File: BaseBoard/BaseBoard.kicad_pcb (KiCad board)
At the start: 2 copper layers, 100 x 86 mm, 48 parts, among them J1 Raspberry_Pi_2_3, J10 Conn_01x01, J11 Conn_01x01, J12 Conn_01x02_Female, J13 Conn_01x02_Female, J14 Conn_01x02_Female, J15 USB_C_Receptacle_USB2.0, J16 Conn_01x02_Female, J17 MOTOR, J18 MOTOR, J19 MOTOR, J2 Longan_A, J20 MOTOR, J21 Conn_01x01, J22 Conn_01x01, J23 IMU, J3 TB6612_A, J4 TB6612_A, J5 Longan_C, J6 Longan_B, J7 TB6612_B, J8 TB6612_B, J9 Conn_02x04, U1 SY6912, U2 CH224K

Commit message: v2板临时提交
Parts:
- removed J11: Conn_01x01, Connector_PinHeader_2.54mm:PinHeader_1x01_P2.54mm_Vertical
- removed J12, J13: Conn_01x02_Female, Connector_Molex:Molex_Mini-Fit_Jr_5566-02A_2x01_P4.20mm_Vertical
- removed J17, J18, J19, J20: MOTOR, Connector_JST:JST_PH_B6B-PH-K_1x06_P2.00mm_Vertical
- removed J6: Longan_B, Connector_PinSocket_2.54mm:PinSocket_1x18_P2.54mm_Vertical
- removed U1: SY6912, Package_SO:HSOP-8-1EP_3.9x4.9mm_P1.27mm_EP2.41x3.1mm_ThermalVias
- added C10: 100nF, Capacitor_SMD:C_0805_2012Metric, F.Cu at (169.7, 30.6)
- added C11: 10uF, Capacitor_SMD:CP_Elec_4x5.4, F.Cu at (139.5, 135.8)
- added C12: 100nF, Capacitor_SMD:C_0805_2012Metric, F.Cu at (134.5, 135.7)
- added C13: 10uF, Capacitor_SMD:CP_Elec_4x5.4, F.Cu at (139.5, 128.4)
- added C14: 100nF, Capacitor_SMD:C_0805_2012Metric, F.Cu at (134.5, 131.6)
- added C15: 10uF, Capacitor_SMD:CP_Elec_4x5.4, F.Cu at (139.5, 121.4)
- added C16: 100nF, Capacitor_SMD:C_0805_2012Metric, F.Cu at (134.5, 121.6)
- added C17: 10uF, Capacitor_SMD:CP_Elec_4x5.4, F.Cu at (139.5, 114.4)
- added C18: 100nF, Capacitor_SMD:C_0805_2012Metric, F.Cu at (134.5, 114.6)
- added C19: 6pF, Capacitor_SMD:C_0603_1608Metric, F.Cu at (131.6, 96.7)
- added C20: 6pF, Capacitor_SMD:C_0603_1608Metric, F.Cu at (178.0, 129.1)
- added C21: 6pF, Capacitor_SMD:C_0603_1608Metric, F.Cu at (129.3, 96.7)
- added C22: 6pF, Capacitor_SMD:C_0603_1608Metric, F.Cu at (185.2, 128.9)
- added C23: 100nF, Capacitor_SMD:C_0805_2012Metric, F.Cu at (173.4, 133.7)
- added C24: 100nF, Capacitor_SMD:C_0805_2012Metric, F.Cu at (180.3, 142.7)
- added C25: 100nF, Capacitor_SMD:C_0805_2012Metric, F.Cu at (173.4, 130.7)
- added C26: 100nF, Capacitor_SMD:C_0805_2012Metric, F.Cu at (158.7, 141.8)
- added C27: 100nF, Capacitor_SMD:C_0805_2012Metric, F.Cu at (175.9, 142.7)
- added C28: 100nF, Capacitor_SMD:C_0805_2012Metric, F.Cu at (158.7, 144.8)
- added C5: 105, Capacitor_SMD:C_0805_2012Metric, F.Cu at (141.1, 78.1)
- added C6: 220uF, Capacitor_SMD:CP_Elec_8x10, F.Cu at (147.2, 74.7)
- added C7: 33nF, Capacitor_SMD:C_0805_2012Metric, F.Cu at (160.9, 91.2)
- added C8: 220uF, Capacitor_SMD:CP_Elec_8x10, F.Cu at (139.3, 95.2)
- added C9: 105, Capacitor_SMD:C_0805_2012Metric, F.Cu at (145.8, 91.6)
- added D4: SS54, Diode_SMD:D_SMB, F.Cu at (156.3, 76.0)
- added D5: LED_Red, LED_SMD:LED_0805_2012Metric, F.Cu at (208.6, 100.6)
- added K1: G5LE-1, Relay_THT:Relay_SPDT_Omron-G5LE-1, F.Cu at (102.5, 79.7)
- added L2: 33uH, Inductor_SMD:L_10.4x10.4_H4.8, F.Cu at (157.5, 83.9)
- added R10: 100k, Resistor_SMD:R_0805_2012Metric, F.Cu at (127.0, 94.2)
- added R11: 360k, Resistor_SMD:R_0805_2012Metric, F.Cu at (122.5, 97.2)
- added R12: 5.1k, Resistor_SMD:R_0805_2012Metric, F.Cu at (177.5, 112.1)
- added R13: 22R, Resistor_SMD:R_0805_2012Metric, F.Cu at (177.5, 115.1)
- added R14: 22R, Resistor_SMD:R_0805_2012Metric, F.Cu at (170.6, 123.5)
- added R15: 10k, Resistor_SMD:R_0805_2012Metric, F.Cu at (181.9, 112.1)
- added R16: 10k, Resistor_SMD:R_0805_2012Metric, F.Cu at (177.5, 118.0)
- added R17: 0, Resistor_SMD:R_0805_2012Metric, F.Cu at (181.9, 115.1)
- added R18: 0, Resistor_SMD:R_0805_2012Metric, F.Cu at (175.0, 123.5)
- added R19: 10k, Resistor_SMD:R_0805_2012Metric, F.Cu at (186.3, 112.1)
- added R20: 10k, Resistor_SMD:R_0805_2012Metric, F.Cu at (181.9, 118.0)
- added R8: 28k, Resistor_SMD:R_0805_2012Metric, F.Cu at (157.1, 91.2)
- added R9: 2k, Resistor_SMD:R_0805_2012Metric, F.Cu at (153.8, 91.2)
- added SW1: SW_Push, Button_Switch_SMD:SW_SPST_TL3342, F.Cu at (156.4, 65.8)
- added SW2: SW_Push, Button_Switch_SMD:SW_SPST_TL3342, F.Cu at (147.2, 65.8)
- added U3: XL4005, Package_TO_SOT_SMD:TO-263-5_TabPin3, F.Cu at (143.3, 84.9)
- added U4: TB6612FNG, Package_SO:SSOP-24_5.3x8.2mm_P0.65mm, F.Cu at (126.5, 118.6)
- added U5: TB6612FNG, Package_SO:SSOP-24_5.3x8.2mm_P0.65mm, F.Cu at (126.5, 132.6)
- added U6: GD32VF103Cx, Package_QFP:LQFP-48_7x7mm_P0.5mm, F.Cu at (128.5, 103.6)
- added Y1: 32.768k, Crystal:Crystal_C38-LF_D3.0mm_L8.0mm_Horizontal, F.Cu at (131.5, 93.6)
- added Y2: 8Mhz, Crystal:Crystal_SMD_5032-2Pin_5.0x3.2mm, F.Cu at (182.6, 124.8)
- C2: value 470nF -> 1uF
- C3: value 10uF/X7R -> 470nF
- C4: value 1uF -> 10uF/X7R
- J10: value Conn_01x01 -> MOTOR; footprint Connector_PinHeader_2.54mm:PinHeader_1x01_P2.54mm_Vertical -> Connector_JST:JST_PH_B6B-PH-K_1x06_P2.00mm_Vertical
- J14: footprint Connector_AMASS:AMASS_XT60-M_1x02_P7.20mm_Vertical -> Connector_Molex:Molex_Mini-Fit_Jr_5566-02A_2x01_P4.20mm_Vertical
- J15: value USB_C_Receptacle_USB2.0 -> Conn_01x02_Female; footprint Connector_USB:USB_C_Receptacle_HRO_TYPE-C-31-M-12 -> Connector_Molex:Molex_Mini-Fit_Jr_5566-02A_2x01_P4.20mm_Vertical
- J16: footprint Connector_Molex:Molex_Mini-Fit_Jr_5566-02A_2x01_P4.20mm_Vertical -> Connector_AMASS:AMASS_XT60-M_1x02_P7.20mm_Vertical
- J2: value Longan_A -> USB_C_Receptacle_USB2.0; footprint Connector_PinSocket_2.54mm:PinSocket_1x18_P2.54mm_Vertical -> Connector_USB:USB_C_Receptacle_HRO_TYPE-C-31-M-12
- J21: value Conn_01x01 -> Conn_01x02_Female; footprint Connector_PinHeader_2.54mm:PinHeader_1x01_P2.54mm_Vertical -> Connector_Molex:Molex_Mini-Fit_Jr_5566-02A_2x01_P4.20mm_Vertical
- J22: value Conn_01x01 -> USB_C_Receptacle_USB2.0; footprint Connector_PinHeader_2.54mm:PinHeader_1x01_P2.54mm_Vertical -> Connector_USB:USB_C_Receptacle_HRO_TYPE-C-31-M-12
- J3: value TB6612_A -> Conn_01x04; footprint Connector_PinSocket_2.54mm:PinSocket_1x08_P2.54mm_Vertical -> Connector_JST:JST_PH_B4B-PH-K_1x04_P2.00mm_Vertical
- J4: value TB6612_A -> MOTOR; footprint Connector_PinSocket_2.54mm:PinSocket_1x08_P2.54mm_Vertical -> Connector_JST:JST_PH_B6B-PH-K_1x06_P2.00mm_Vertical
- J5: value Longan_C -> Barrel_Jack_Switch; footprint Connector_PinSocket_2.54mm:PinSocket_2x04_P2.54mm_Vertical -> Connector_BarrelJack:BarrelJack_Wuerth_6941xx301002
- J7, J8: value TB6612_B -> MOTOR; footprint Connector_PinSocket_2.54mm:PinSocket_1x08_P2.54mm_Vertical -> Connector_JST:JST_PH_B6B-PH-K_1x06_P2.00mm_Vertical
- R1: value 25mR -> 1k; footprint Resistor_SMD:R_1206_3216Metric -> Resistor_SMD:R_0805_2012Metric
- R2: value 10k -> 25mR; footprint Resistor_SMD:R_0805_2012Metric -> Resistor_SMD:R_1206_3216Metric
- R5: value 10k -> 56k
- R6: value 56k -> 10k
- U2: value CH224K -> SY6912; footprint Custom:ESSOP10 -> Package_SO:HSOP-8-1EP_3.9x4.9mm_P1.27mm_EP2.41x3.1mm_ThermalVias
- moved J9 92.6 mm to (139.2, 64.5)
- moved J21 76.0 mm to (193.9, 65.8), turned to 90 degrees
- moved D2 72.9 mm to (173.0, 23.7), turned to 0 degrees
- moved L1 72.5 mm to (154.5, 30.6)
- moved JP1 72.0 mm to (173.6, 20.4), turned to 0 degrees
- moved D1 69.9 mm to (145.1, 50.1), turned to 0 degrees
- moved J2 67.5 mm to (123.5, 64.6), turned to 180 degrees
- moved J10 65.6 mm to (133.5, 145.6)
- moved R2 65.1 mm to (151.6, 42.1)
- moved J3 64.9 mm to (186.5, 101.6), turned to 0 degrees
- moved D3 63.4 mm to (146.9, 46.3)
- moved J22 62.4 mm to (182.8, 64.7)
- moved R4 62.3 mm to (169.4, 37.0)
- moved C1 58.9 mm to (160.5, 37.0)
- moved C4 54.6 mm to (153.2, 45.3), turned to 0 degrees
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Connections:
- C1 pad 1: /VBCHG -> +BATT
- C3 pad 1: /VCHARGE -> GND
- C3 pad 2: GND -> Net-(C3-Pad2)
- C4 pad 1: GND -> /Power/VCHARGE
- C4 pad 2: Net-(C4-Pad2) -> GND
- D3 pad 1: /VCHARGE -> /Power/VCHARGE
- J1 pad 21: Net-(J1-Pad21) -> /LIDAR_TX
- J1 pad 24: Net-(J1-Pad24) -> /LIDAR_RX
- J10 pad 1: GND -> /Motor/MOT4_N
- J14 pad 1: GND -> /Power/CTRL
- J14 pad 2: /VBAT -> +12V
- J16 pad 1: VBUS -> GND
- J16 pad 2: GND -> +BATT
- J21 pad 1: GND -> VBUS
- J3 pad 1: +12V -> +5V
- J3 pad 2: +3V3 -> /LIDAR_RX
- J3 pad 3: GND -> /LIDAR_TX
- J3 pad 4: /MOT1_N -> GND
- J4 pad 1: +12V -> /Motor/MOT1_N
- J4 pad 2: +3V3 -> /Motor/MOT1_P
- J4 pad 3: GND -> /ENC1_B
- J4 pad 4: /MOT3_N -> +3V3
- J4 pad 5: /MOT3_P -> /ENC1_A
- J4 pad 6: /MOT4_P -> GND
- J5 pad 1: GND -> +BATT
- J5 pad 2: /ENC4_B -> GND
- J5 pad 3: /PWM2 -> GND
- J7 pad 1: /PWM1 -> /Motor/MOT2_N
- J7 pad 2: /MOT1_C2 -> /Motor/MOT2_P
- J7 pad 3: /MOT1_C1 -> /ENC2_B
- J7 pad 5: /MOT2_C1 -> /ENC2_A
- J7 pad 6: /MOT2_C2 -> GND
- J8 pad 1: /PWM3 -> /Motor/MOT3_N
- J8 pad 2: /MOT3_C2 -> /Motor/MOT3_P
- J8 pad 3: /MOT3_C1 -> /ENC3_B
- J8 pad 5: /MOT4_C1 -> /ENC3_A
- J8 pad 6: /MOT4_C2 -> GND
- JP1 pad 1: /VCHARGE -> /Power/VCHARGE
- L1 pad 2: /RS -> /Power/RS
- R1 pad 1: /RS -> Net-(C2-Pad2)
- R1 pad 2: /VBCHG -> VBUS
- R2 pad 1: Net-(R2-Pad1) -> /Power/RS
- R2 pad 2: /VCHARGE -> +BATT
- R3 pad 1: GND -> Net-(R3-Pad1)
- R3 pad 2: Net-(R2-Pad1) -> /Power/VCHARGE
- R4 pad 1: /VCHARGE -> GND
- R4 pad 2: Net-(D1-Pad2) -> Net-(R3-Pad1)
- R5 pad 1: Net-(C4-Pad2) -> GND
- R5 pad 2: VBUS -> Net-(R5-Pad2)
- R6 pad 1: GND -> VBUS
- R7 pad 1: VBUS -> /Power/VCHARGE
- R7 pad 2: Net-(R7-Pad2) -> Net-(D1-Pad2)
- U2 pad 1: Net-(C4-Pad2) -> Net-(C3-Pad2)
- U2 pad 2: Net-(U2-Pad2) -> /Power/RS
- U2 pad 3: Net-(U2-Pad3) -> +BATT
- U2 pad 4: /DP -> Net-(R3-Pad1)
- U2 pad 5: /DM -> Net-(JP1-Pad2)
- U2 pad 6: /CC2 -> Net-(D1-Pad1)
- U2 pad 7: /CC1 -> Net-(L1-Pad1)
- U2 pad 8: Net-(R7-Pad2) -> /Power/VCHARGE
- U2 pad 9: Net-(R6-Pad2) -> GND
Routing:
- net +3V3: track 232.1 -> 0.16 mm, vias 6 -> 0
- net /ENC4_B: track 139.2 -> 0.00 mm
- net /ENC4_A: track 134.0 -> 0.00 mm
- net +12V: track 172.4 -> 47.7 mm
- net /ENC3_A: track 104.7 -> 0.00 mm, vias 1 -> 0
- net /ENC3_B: track 102.9 -> 0.00 mm, vias 1 -> 0
- net /PWM3: track 100.5 -> 0.00 mm, vias 2 -> 0
- net /ENC2_B: track 98.2 -> 0.00 mm, vias 1 -> 0
- net /ENC2_A: track 96.3 -> 0.00 mm, vias 1 -> 0
- net /ENC1_B: track 91.8 -> 0.00 mm, vias 1 -> 0
- net /ENC1_A: track 86.6 -> 0.00 mm, vias 1 -> 0
- net /PWM2: track 81.1 -> 0.00 mm, vias 2 -> 0
- net /DEBUG_RX: track 78.3 -> 0.00 mm, vias 1 -> 0
- net /DEBUG_TX: track 68.5 -> 0.00 mm, vias 1 -> 0
- net /PWM1: track 69.9 -> 9.57 mm, vias 1 -> 0
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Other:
- net class Default: trace_width 0.4 -> 0.25
- board text removed: "-"

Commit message: v2提交
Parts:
- removed JP1: SolderJumper_3_Open, Jumper:SolderJumper-3_P1.3mm_Open_Pad1.0x1.5mm_NumberLabels
- added C29: 10uF, Capacitor_SMD:C_0603_1608Metric, F.Cu at (169.8, 87.4)
- added C30: 100pF, Capacitor_SMD:C_0402_1005Metric, F.Cu at (172.2, 87.4)
- added C31: 1uF, Capacitor_SMD:C_0402_1005Metric, F.Cu at (173.1, 75.2)
- added C32: 470uF, Capacitor_SMD:CP_Elec_10x10.5, F.Cu at (193.3, 76.4)
- added C33: 1uF, Capacitor_SMD:C_0402_1005Metric, F.Cu at (145.8, 100.3)
- added C34: 1uF, Capacitor_SMD:C_0402_1005Metric, F.Cu at (145.8, 102.3)
- added G***: LOGO, Customv2:Linux_12x12, F.Cu at (204.5, 108.7)
- added G***: LOGO, Customv2:ROS_LOGO_20x6, F.Cu at (203.2, 129.9)
- added G***: LOGO, Customv2:Anaheim_Electronic_20, F.Cu at (172.1, 125.9)
- added Q1: 9926A, Package_SO:SO-8_3.9x4.9mm_P1.27mm, F.Cu at (177.6, 90.3)
- added R21: 1.6k, Resistor_SMD:R_0603_1608Metric, F.Cu at (170.0, 76.5)
- added R22: 95.3k, Resistor_SMD:R_0603_1608Metric, F.Cu at (174.1, 78.4)
- added R23: 910k, Resistor_SMD:R_0603_1608Metric, F.Cu at (174.1, 76.9)
- added R24: 1k, Resistor_SMD:R_0402_1005Metric, F.Cu at (172.2, 88.6)
- added R25: 0.02R, Resistor_SMD:R_2512_6332Metric, F.Cu at (170.0, 91.1)
- added R26: 0.05R/2W, Resistor_SMD:R_2512_6332Metric, F.Cu at (191.8, 89.2)
- added U1: CH224K, Customv2:ESSOP10, F.Cu at (179.8, 73.8)
- added U7: XC6206PxxxMR, Package_TO_SOT_SMD:SOT-23, F.Cu at (143.3, 101.6)
- C1: value 10uF/X7R -> 100uF; footprint Capacitor_SMD:C_0805_2012Metric -> Capacitor_SMD:CP_Elec_6.3x7.7
- C10, C12, C14, C16, C18, C2, C23, C24, C25, C26, C27, C28, C7: footprint Capacitor_SMD:C_0805_2012Metric -> Capacitor_SMD:C_0402_1005Metric
- C19, C20, C21, C22: footprint Capacitor_SMD:C_0603_1608Metric -> Capacitor_SMD:C_0402_1005Metric
- C3: value 470nF -> 22nF; footprint Capacitor_SMD:C_0805_2012Metric -> Capacitor_SMD:C_0402_1005Metric
- C4: value 10uF/X7R -> 470nF; footprint Capacitor_SMD:C_0805_2012Metric -> Capacitor_SMD:C_0402_1005Metric
- C5, C9: value 105 -> 1uF; footprint Capacitor_SMD:C_0805_2012Metric -> Capacitor_SMD:C_0402_1005Metric
- D3: value SS34 -> SS54; footprint Diode_SMD:D_SMA -> Diode_SMD:D_SMB
- D5: value LED_Red -> LED_White
- J9: footprint Connector_PinHeader_2.54mm:PinHeader_2x04_P2.54mm_Vertical -> Connector_PinHeader_2.54mm:PinHeader_1x04_P2.54mm_Vertical
- K1: value G5LE-1 -> SRD-12V
- L1: value 2.2uH -> 4.7uH
- R1, R10, R12, R13, R14, R15, R16, R17, R18, R19, R20, R4, R6, R7: footprint Resistor_SMD:R_0805_2012Metric -> Resistor_SMD:R_0402_1005Metric
- R11, R8, R9: footprint Resistor_SMD:R_0805_2012Metric -> Resistor_SMD:R_0603_1608Metric
- R2: value 25mR -> 820k; footprint Resistor_SMD:R_1206_3216Metric -> Resistor_SMD:R_0603_1608Metric
- R3: value 10k -> 95.3k; footprint Resistor_SMD:R_0805_2012Metric -> Resistor_SMD:R_0603_1608Metric
- R5: value 56k -> 24k; footprint Resistor_SMD:R_0805_2012Metric -> Resistor_SMD:R_0402_1005Metric
- U2: value SY6912 -> CN3306; footprint Package_SO:HSOP-8-1EP_3.9x4.9mm_P1.27mm_EP2.41x3.1mm_ThermalVias -> Package_SO:TSSOP-16_4.4x5mm_P0.65mm
- Y1: footprint Crystal:Crystal_C38-LF_D3.0mm_L8.0mm_Horizontal -> Crystal:Crystal_SMD_3215-2Pin_3.2x1.5mm
- Y2: footprint Crystal:Crystal_SMD_5032-2Pin_5.0x3.2mm -> Crystal:Crystal_SMD_3225-4Pin_3.2x2.5mm
- moved C24 75.7 mm to (122.3, 94.1), turned to 90 degrees
- moved R12 71.6 mm to (118.8, 71.1)
- moved R13 70.7 mm to (122.0, 71.1)
- moved R14 69.4 mm to (125.0, 71.1), turned to 180 degrees
- moved C22 67.0 mm to (127.0, 95.7), turned to 180 degrees
- moved R19 65.1 mm to (123.7, 94.4), turned to 270 degrees
- moved C27 64.4 mm to (122.7, 106.5), turned to 90 degrees
- moved Y2 64.0 mm to (127.0, 93.1), turned to 270 degrees
- moved C20 63.9 mm to (127.0, 90.6)
- moved C28 63.3 mm to (123.7, 92.0), turned to 90 degrees
- moved R17 61.0 mm to (123.8, 96.4)
- moved R18 59.4 mm to (122.3, 96.1), turned to 270 degrees
- moved D3 59.1 mm to (185.9, 90.7), turned to 180 degrees
- moved L1 57.4 mm to (177.2, 83.4), turned to 270 degrees
- moved R16 57.2 mm to (122.0, 104.1), turned to 180 degrees
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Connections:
- C1 pad 1: +BATT -> VBUS
- C26 pad 1: +3V3 -> /VSSA
- C26 pad 2: GND -> /VDDA
- C3 pad 1: GND -> Net-(C3-Pad1)
- C3 pad 2: Net-(C3-Pad2) -> GND
- C4 pad 1: /Power/VCHARGE -> Net-(C4-Pad1)
- D2 pad 1: GND -> Net-(D2-Pad1)
- D2 pad 2: Net-(D1-Pad1) -> Net-(D2-Pad2)
- D3 pad 1: /Power/VCHARGE -> Net-(C32-Pad1)
- D3 pad 2: VBUS -> Net-(D3-Pad2)
- D5 pad 2: +3V3 -> Net-(D5-Pad2)
- J2 pad A4: +5VA -> +5V
- J2 pad A9: +5VA -> +5V
- J2 pad B4: +5VA -> +5V
- J2 pad B9: +5VA -> +5V
- J9 pad 1: /ENC4_B -> GND
- J9 pad 2: GND -> /DEBUG_RX
- J9 pad 3: /ENC4_A -> /DEBUG_TX
- J9 pad 4: /DEBUG_RX -> +3V3
- L1 pad 1: Net-(L1-Pad1) -> VBUS
- L1 pad 2: /Power/RS -> Net-(D3-Pad2)
- R13 pad 1: /USB_DM -> /PWM4
- R2 pad 1: /Power/RS -> VBUS
- R2 pad 2: +BATT -> Net-(R2-Pad2)
- R20 pad 1: Net-(D5-Pad1) -> +3V3
- R20 pad 2: Net-(R20-Pad2) -> Net-(D5-Pad2)
- R3 pad 1: Net-(R3-Pad1) -> Net-(R2-Pad2)
- R3 pad 2: /Power/VCHARGE -> GND
- R4 pad 1: GND -> VBUS
- R4 pad 2: Net-(R3-Pad1) -> Net-(D2-Pad2)
- R7 pad 1: /Power/VCHARGE -> VBUS
- U2 pad 1: Net-(C3-Pad2) -> Net-(R22-Pad1)
- U2 pad 2: /Power/RS -> Net-(C3-Pad1)
- U2 pad 3: +BATT -> Net-(R2-Pad2)
- U2 pad 4: Net-(R3-Pad1) -> Net-(U2-Pad4)
- U2 pad 5: Net-(JP1-Pad2) -> GND
- U2 pad 7: Net-(L1-Pad1) -> Net-(D2-Pad1)
- U2 pad 8: /Power/VCHARGE -> Net-(C32-Pad1)
- U2 pad 9: GND -> +BATT
- U6 pad 2: Net-(R20-Pad2) -> Net-(D5-Pad1)
- U6 pad 33: Net-(U6-Pad33) -> /USB_DP
- Y2 pad 2: /OSCOUT -> GND
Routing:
- net +3V3: track 0.16 -> 257.7 mm, vias 0 -> 15
- net GND: track 37.4 -> 185.3 mm, vias 0 -> 34
- net +12VA: track 0.00 -> 145.6 mm, vias 0 -> 7
- net +5V: track 40.9 -> 134.6 mm, vias 0 -> 5
- net Net-(D5-Pad1): track 0.00 -> 92.5 mm, vias 0 -> 2
- net /BOOT0: track 0.00 -> 80.9 mm, vias 0 -> 4
- net VBUS: track 0.00 -> 80.6 mm
- net /PWM4: track 0.00 -> 76.4 mm, vias 0 -> 6
- net +BATT: track 43.1 -> 112.6 mm, vias 0 -> 2
- net Net-(C28-Pad1): track 0.00 -> 58.1 mm
- net /DEBUG_RX: track 0.00 -> 57.3 mm, vias 0 -> 2
- net /DEBUG_TX: track 0.00 -> 55.2 mm, vias 0 -> 2
- net /ADC: track 0.00 -> 51.3 mm, vias 0 -> 2
- net /CTL_TX: track 0.69 -> 50.4 mm, vias 0 -> 2
- net /CTL_RX: track 0.69 -> 49.7 mm, vias 0 -> 2
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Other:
- net class Power: clearance 0.3 -> 0.2
- net class Power2: clearance 0.3 -> 0.2
- board text added: "3V3 TX RX GND"
- board text added: "AE-87 Lite, Powered by ROS"
- board text added: "Boot0"
- board text added: "GND ENCA 3V3 ENCB MOT+ MOT-"
- board text added: "GND TX RX 5V"
- board text added: "Lidar"
- board text added: "Reset"
- board text added: "Stop"
- board text added: "Work Charge Full"
- board text added: "©2021 ESAC Rpi Motor Hat v2"
- board text removed: "+ -"
- board text removed: "Emergency"
- board text removed: "MOT- MOT+ ENC_B 3V3 ENC_A GND"
- board text removed: "NC: 11.1v 1-2: 7.4v 2-3: 3.7v"
- board text removed: "Rpi Motor Hat ©2021 ESAC"
- board text removed: "TMS TCK JDI JDO 3V3 TX RX GND"

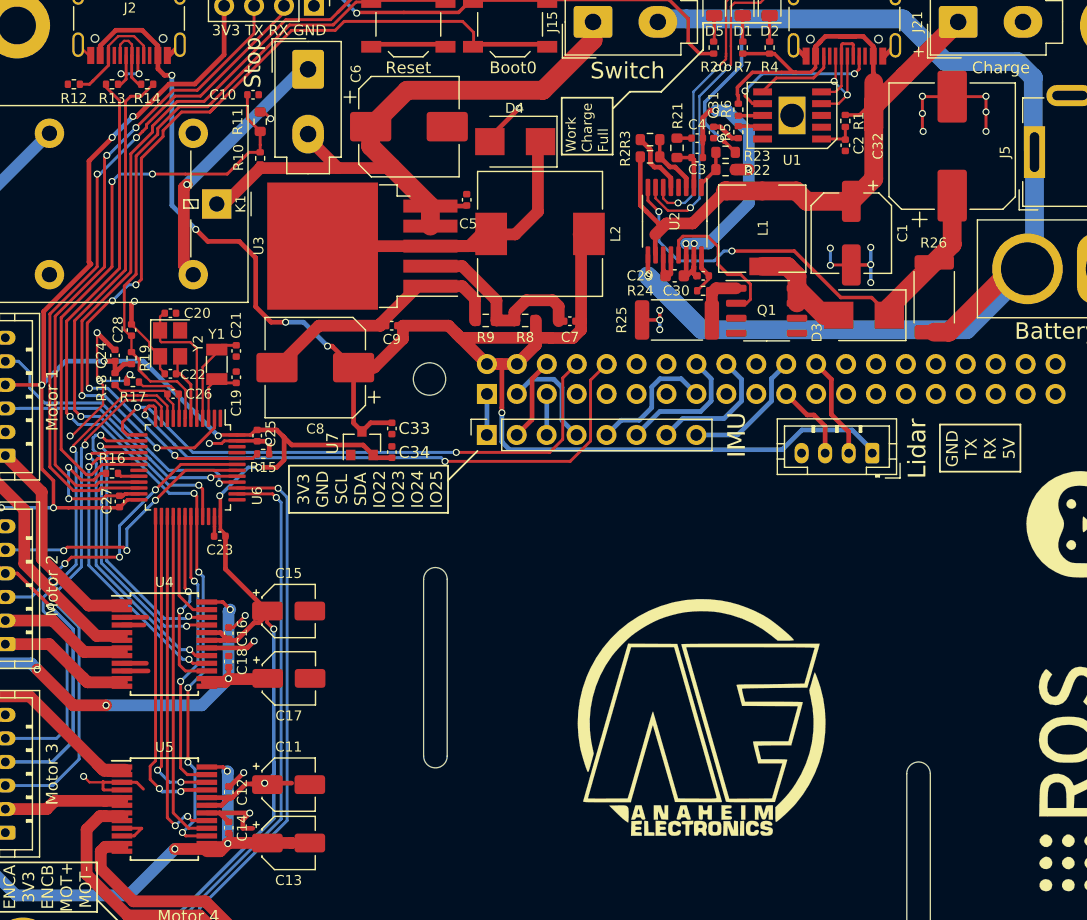
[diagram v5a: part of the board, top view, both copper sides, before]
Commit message: Modify some footprints.
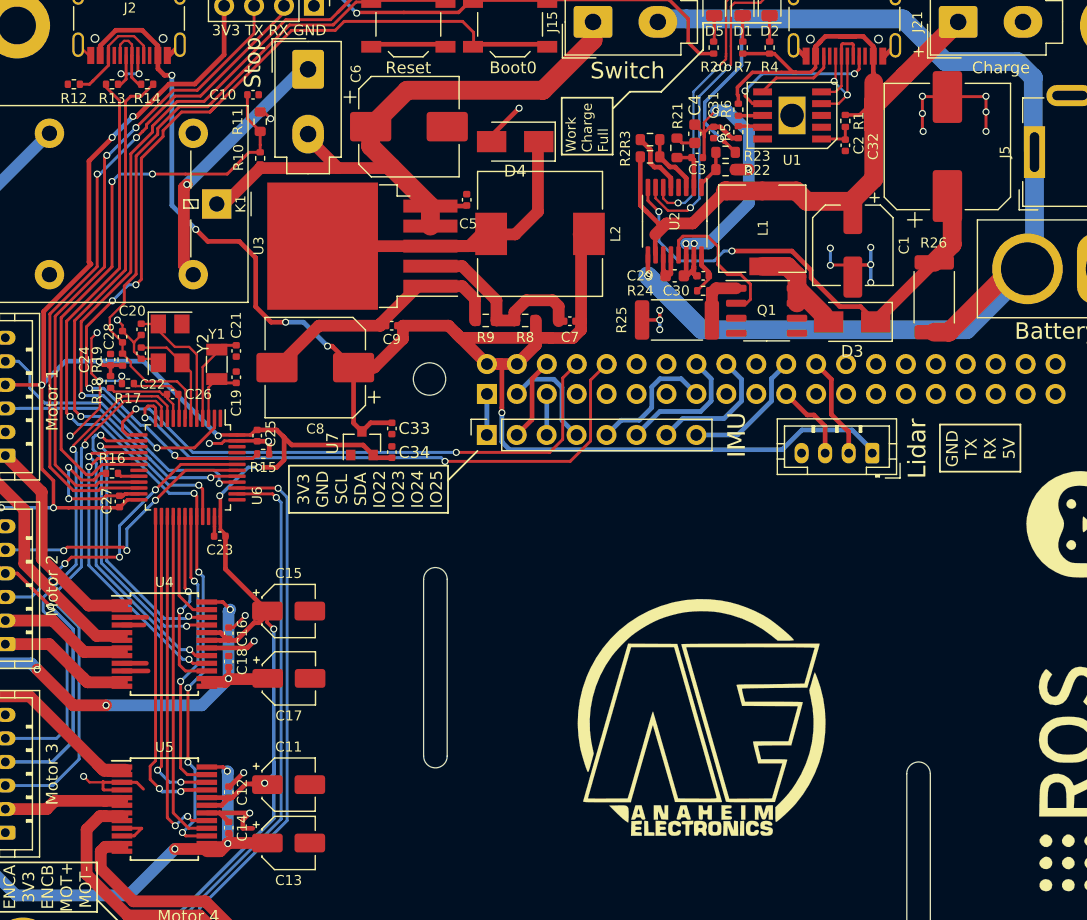
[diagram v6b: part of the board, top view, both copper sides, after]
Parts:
- C4: footprint Capacitor_SMD:C_0402_1005Metric -> Capacitor_SMD:C_0603_1608Metric
- D3, D4: footprint Diode_SMD:D_SMB -> Diode_SMD:D_SMA
- Y2: footprint Crystal:Crystal_SMD_3225-4Pin_3.2x2.5mm -> Crystal:Crystal_SMD_5032-4Pin_5.0x3.2mm
- moved C22 3.03 mm to (124.5, 93.9), turned to 270 degrees
- moved C20 2.83 mm to (124.5, 91.9), turned to 270 degrees
- moved D3 1.15 mm to (184.9, 91.3)
- moved C1 1.04 mm to (184.9, 84.8)
- moved C28 0.95 mm to (122.9, 92.5)
- moved R19 0.77 mm to (122.9, 94.5)
- moved C24 0.52 mm to (121.9, 94.5)
- moved R18 0.46 mm to (121.9, 96.4)
- moved R17 0.45 mm to (123.4, 96.5)
- moved C4 0.42 mm to (171.5, 75.3), turned to 90 degrees
- moved C32 0.41 mm to (192.9, 76.4)
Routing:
- net /OSCOUT: track 6.07 -> 9.32 mm
- net +3V3: track 257.7 -> 254.8 mm
- net +12VA: track 145.6 -> 143.6 mm
- net Net-(C28-Pad1): track 58.1 -> 59.5 mm
- net Net-(D3-Pad2): track 12.4 -> 11.1 mm
- net /OSCIN: track 11.9 -> 12.7 mm
- net Net-(C32-Pad1): track 40.2 -> 40.7 mm

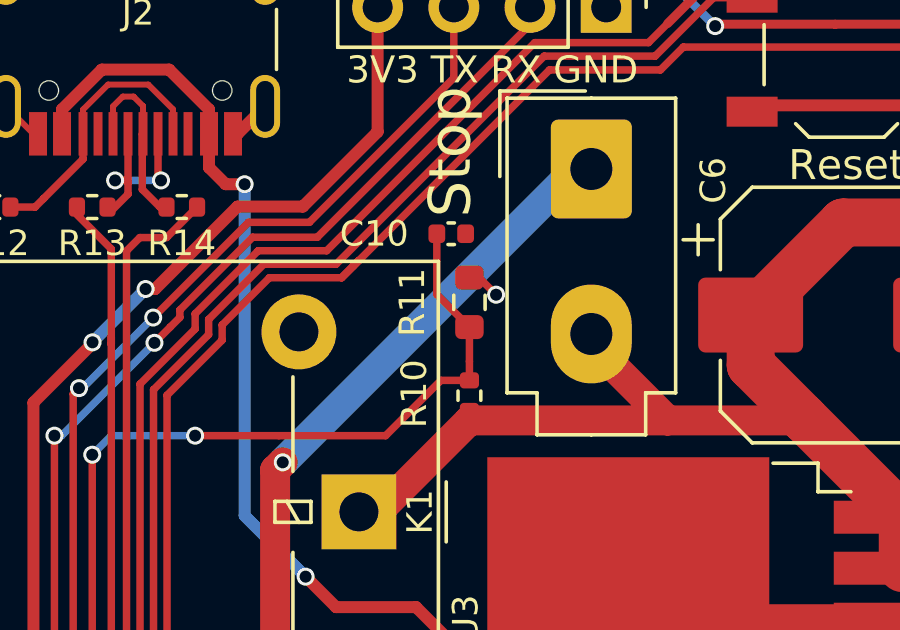
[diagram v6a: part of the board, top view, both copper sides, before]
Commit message: 修正两处电阻阻值不正确的问题
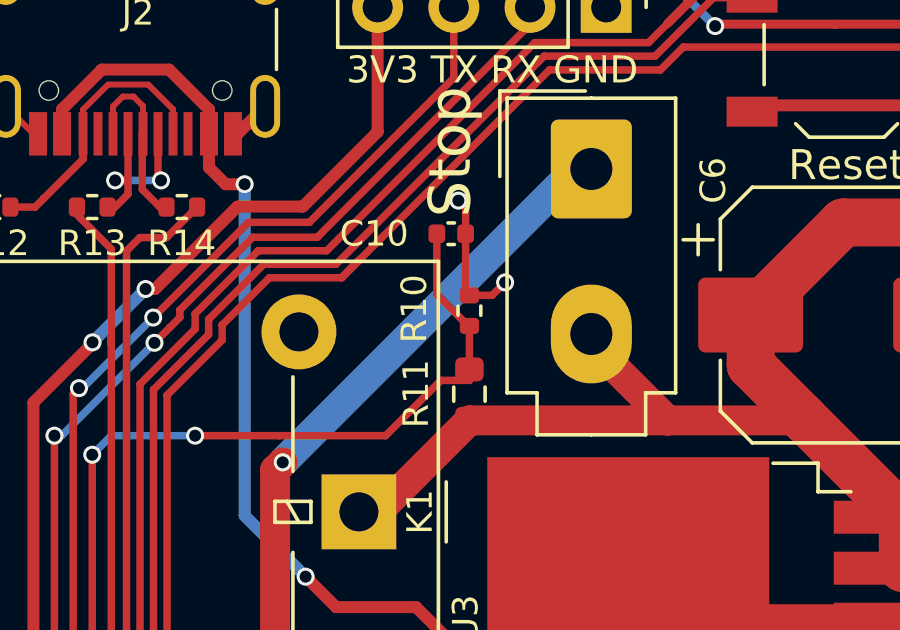
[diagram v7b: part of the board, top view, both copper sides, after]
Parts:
- R8: value 28k -> 10.5k
- moved R11 3.06 mm to (134.6, 77.4)
- moved R10 2.83 mm to (134.6, 74.6)
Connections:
- R10 pad 1: +12V -> /ADC
- R10 pad 2: /ADC -> GND
- R11 pad 1: /ADC -> +12V
- R11 pad 2: GND -> /ADC
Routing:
- net GND: track 185.3 -> 188.9 mm, vias 34 -> 35
